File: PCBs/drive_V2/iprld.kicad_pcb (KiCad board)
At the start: 2 copper layers, 100 x 100 mm, 78 parts, among them IC1 W25Q16JVUXIQ_TR, IC2 ADS1115IDGSR, J1 SM06B-GHS-TB_LF__SN_, J10 XT60PW-F, J11 12401832E402A, J2 SM06B-GHS-TB_LF__SN_, J3 SM06B-GHS-TB_LF__SN_, J4 SM06B-GHS-TB_LF__SN_, J5 SM06B-GHS-TB_LF__SN_, J6 XT60PW-F, J7 SM06B-GHS-TB_LF__SN_, J8 XT60PW-F, J9 XT30PW-F, U1 AMS1117-3.3, U10 USBLC6-4SC6, U11 4N35, U12 4N35, U13 4N35, U14 4N35, U2 ESP32-S3, U3 4N35, U5 TCA9548APWR, U6 4N35, U7 4N35, U8 4N35, U9 AMS1117-5.0, Y1 7M40000010

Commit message: Add files via upload
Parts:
- moved U3 0.40 mm to (41.7, 19.6)
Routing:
- net /+FUSE_R: track 27.0 -> 30.6 mm
- net /+FUSE_L: track 17.9 -> 21.2 mm
- net /VBUS: track 20.4 -> 21.4 mm
- net /D+: track 82.7 -> 83.6 mm

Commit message: Add files via upload
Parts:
- moved D1 3.15 mm to (84.3, 83.8)
- moved U10 3.15 mm to (78.2, 83.6)
- moved J11 3.10 mm to (81.5, 93.8)
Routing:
- net /+FUSE_R: track 30.6 -> 26.6 mm
- net Net-(J11-CC2): track 16.0 -> 19.1 mm
- net GND: track 258.3 -> 261.4 mm
- net /D-: track 84.9 -> 87.2 mm
- net +5V: track 372.4 -> 373.7 mm
- net /D+: track 83.6 -> 84.9 mm
- net Net-(J11-CC1): track 16.8 -> 18.1 mm
- net +3.3V: vias 6 -> 8
- added copper zone on F.Cu, net +5V

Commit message: TEST1 - added a via
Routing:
- net GND: vias 45 -> 46
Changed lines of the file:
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@@
+	)
+	(via
+		(at 51.2 35.7)
+		(size 0.6)
+		(drill 0.3)
+		(layers "F.Cu" "B.Cu")
+		(free yes)
+		(net 1)
 	)
 	(via

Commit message: changed adc components
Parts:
- added C9: 1u, Capacitor_SMD:C_0603_1608Metric, F.Cu at (50.3, 54.8)
- added G***: LOGO, main_lib:IPRL_31mm, F.Cu at (78.0, 65.6)
- added R1: 10k, Resistor_SMD:R_0805_2012Metric, F.Cu at (50.2, 45.5)
- added R8: 10k, Resistor_SMD:R_0805_2012Metric, F.Cu at (50.3, 58.1)
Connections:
- IC2 pad 1: GND -> Net-(IC2-ADDR)
- IC2 pad 2: unconnected-(IC2-ALERT/RDY-Pad2) -> Net-(IC2-ALERT/RDY)
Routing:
- net Net-(IC2-ALERT/RDY): track 0.00 -> 12.2 mm, vias 0 -> 2
- net +3.3V: track 271.9 -> 278.9 mm
- net Net-(IC2-ADDR): track 0.00 -> 6.85 mm
- net GND: track 261.4 -> 256.4 mm

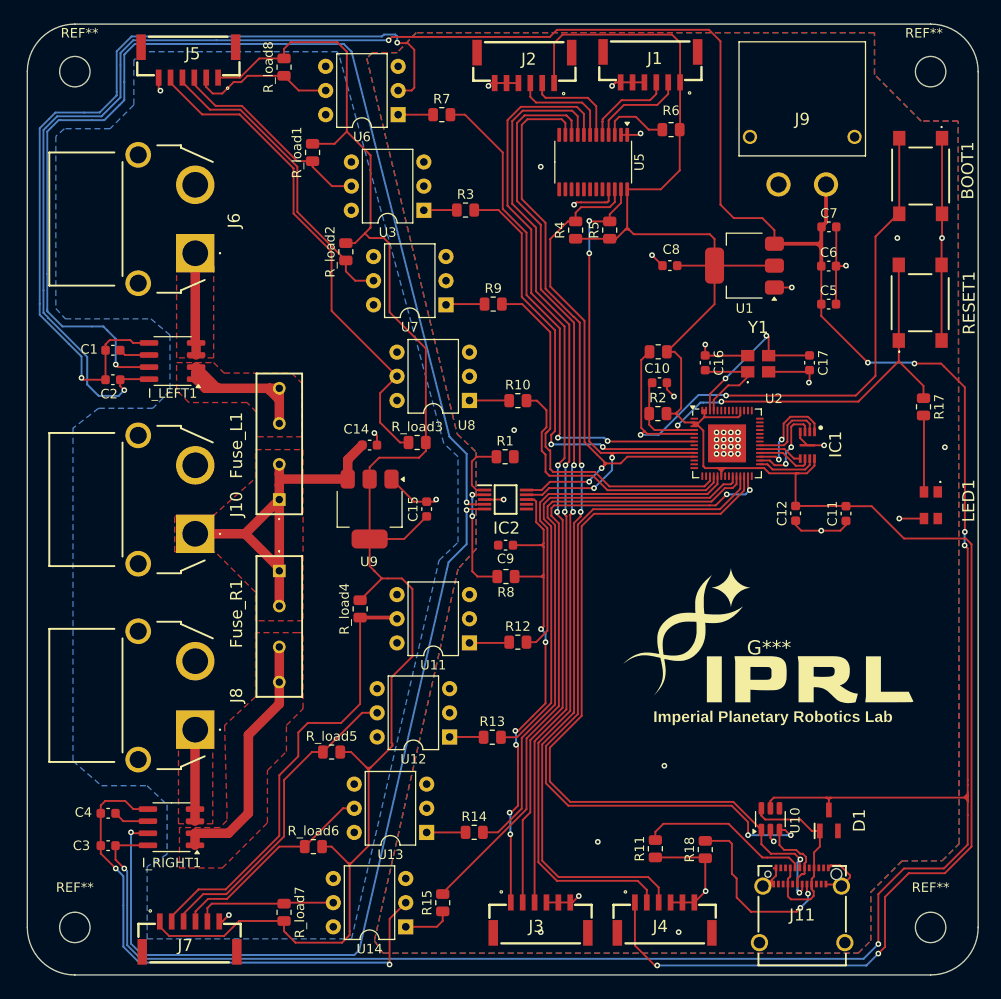
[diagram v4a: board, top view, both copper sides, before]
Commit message: New USB C footprint, changed XT inputs to male
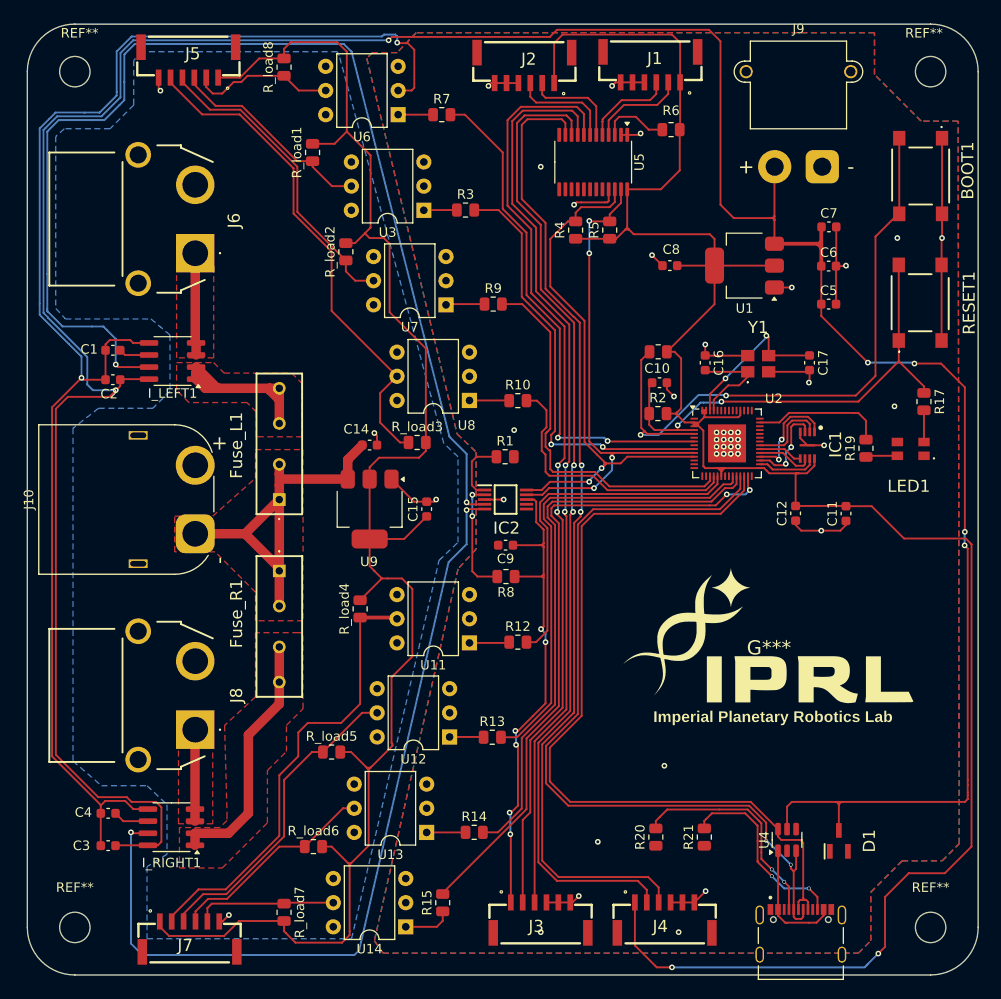
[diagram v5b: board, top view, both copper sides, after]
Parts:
- removed J11: 12401832E402A, iprl_footprints:12401832E402A
- removed R11, R18: 5.1k, Resistor_SMD:R_0805_2012Metric
- removed U10: USBLC6-4SC6, Package_TO_SOT_SMD:SOT-23-6
- added J12: TYPE-C-31-M-12, main_lib:TYPE-C-31-M-12, F.Cu at (81.3, 97.9)
- added R19: 56, Resistor_SMD:R_0805_2012Metric, F.Cu at (88.2, 44.6)
- added R20: 5.1k, Resistor_SMD:R_0805_2012Metric, F.Cu at (66.1, 85.5)
- added R21: 5.1k, Resistor_SMD:R_0805_2012Metric, F.Cu at (71.2, 85.5)
- added U4: USBLC6-4SC6, Package_TO_SOT_SMD:SOT-23-6, F.Cu at (79.9, 85.8)
- J10: footprint iprl_footprints:XT60PWF -> Connector_AMASS:AMASS_XT60PW-M_1x02_P7.20mm_Horizontal
- J9: footprint iprl_footprints:XT30PWF -> Connector_AMASS:AMASS_XT30PW-M_1x02_P2.50mm_Horizontal
- moved LED1 6.29 mm to (92.9, 44.7), turned to 0 degrees
- moved J9 4.96 mm to (83.6, 15.0)
- moved D1 2.39 mm to (85.3, 85.9)
- moved R17 0.55 mm to (94.3, 39.7)
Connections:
- LED1 pad 1: unconnected-(LED1-K_RED-Pad1) -> GND
- LED1 pad 2: unconnected-(LED1-A_RED-Pad2) -> Net-(LED1-A_RED)
- U2 pad 41: unconnected-(U2-GPIO36-Pad41) -> /LED_Red
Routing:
- net +5V: track 373.7 -> 325.1 mm, vias 8 -> 6
- net GND: track 256.4 -> 231.8 mm, vias 46 -> 42
- net Net-(J12-CC1): track 0.00 -> 23.3 mm, vias 0 -> 2
- net Net-(J12-CC2): track 0.00 -> 20.2 mm, vias 0 -> 2
- net Net-(J11-CC2): track 19.1 -> 0.00 mm, vias 2 -> 0
- net Net-(J11-CC1): track 18.1 -> 0.00 mm
- net /LED_Red: track 0.00 -> 13.9 mm
- net /VBUS: track 21.4 -> 12.9 mm
- net Net-(LED1-A_GREEN): track 8.06 -> 3.34 mm
- net Net-(LED1-A_RED): track 0.00 -> 3.35 mm
- net /D+: track 84.9 -> 87.3 mm, vias 2 -> 0
- net /D-: track 87.2 -> 88.8 mm
- net Net-(RESET1-NO_1): track 51.5 -> 51.0 mm
- removed copper zone on F.Cu, net +5V

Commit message: added connector names
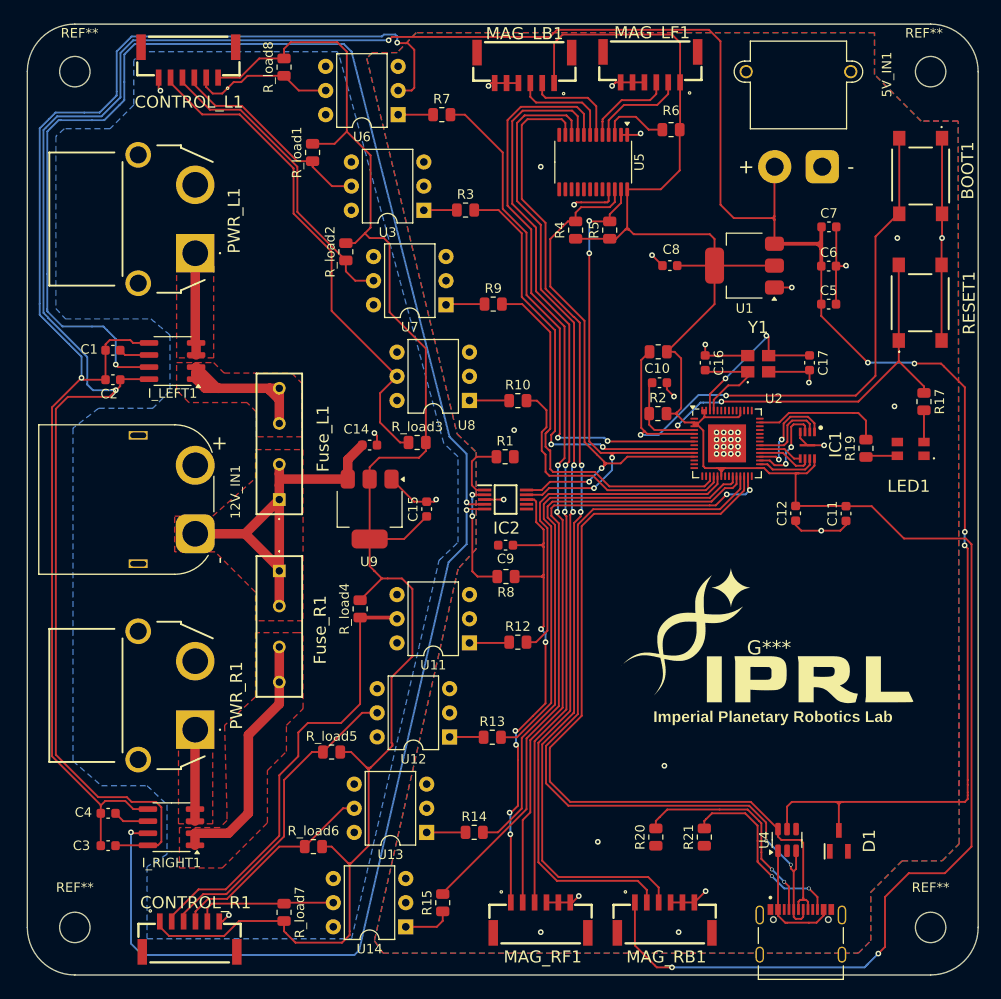
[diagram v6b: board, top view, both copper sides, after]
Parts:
- renumbered J10 to 12V_IN1, J9 to 5V_IN1, J5 to CONTROL_L1, J7 to CONTROL_R1, J2 to MAG_LB1, J1 to MAG_LF1, J4 to MAG_RB1, J3 to MAG_RF1, J6 to PWR_L1, J8 to PWR_R1
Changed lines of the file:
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@@
 		(descr "Connector XT30 Horizontal PCB Male, https://www.tme.eu/Document/6eb2005a51a52592b3f19e8a450c54c8/XT30PW-M.pdf")
 		(tags "RC Connector XT30")
-		(property "Reference" "J9"
-			(at -2.5 -14.5 0)
+		(property "Reference" "5V_IN1"
+			(at 6.8 -9.7 -90)
 			(layer "F.SilkS")
 			(effects
@@
 		(descr "XT60PW-F-4")
 		(tags "Connector")
-		(property "Reference" "J8"
+		(property "Reference" "PWR_R1"
 			(at 3.6 4.3375 -90)
 			(layer "F.SilkS")
@@
 		(descr "SM06B-GHS-TB")
 		(tags "Connector")
-		(property "Reference" "J2"
-			(at 4.91667 -1.78567 180)
+		(property "Reference" "MAG_LB1"
+			(at 5.35 0.9 0)
 			(layer "F.SilkS")
 			(effects
@@
 		(descr "SM06B-GHS-TB")
 		(tags "Connector")
-		(property "Reference" "J7"
-			(at 4.91667 -1.78567 0)
+		(property "Reference" "CONTROL_R1"
+			(at 6.0135 -6.273885 0)
 			(layer "F.SilkS")
 			(effects
@@
 		(descr "SM06B-GHS-TB")
 		(tags "Connector")
-		(property "Reference" "J1"
-			(at 4.91667 -1.78567 180)
+		(property "Reference" "MAG_LF1"
+			(at 5.2 0.926115 180)
 			(layer "F.SilkS")
 			(effects
@@
 		(tags "LED")
 		(property "Reference" "LED1"
-			(at -0.2 3.925 360)
+			(at -0.2 3.925 0)
 			(layer "F.SilkS")
 			(effects
@@
 		)
 		(property "Value" "AAA3528ESGCT"
-			(at 0.25 0 360)
+			(at 0.25 0 0)
 			(layer "F.SilkS")
 			(hide yes)
@@
 		)
 		(fp_text user "${REFERENCE}"
-			(at 0.25 0 360)
+			(at 0.25 0 0)
 			(layer "F.Fab")
 			(effects
@@
 		(tags "Undefined or Miscellaneous")
 		(property "Reference" "Fuse_L1"
-			(at 5.7 -4.5 -90)
+			(at 6.4 4.6 -90)
 			(layer "F.SilkS")
 			(effects
@@
 		(descr "SM06B-GHS-TB")
 		(tags "Connector")
-		(property "Reference" "J5"
-			(at 4.91667 -1.78567 180)
+		(property "Reference" "CONTROL_L1"
+			(at 5.3135 -6.873885 180)
 			(layer "F.SilkS")
 			(effects
@@
 		(descr "Connector XT60 Horizontal PCB Female, https://www.tme.eu/Document/b13629717d44ae038681dba08d18c0b6/XT60PW-M.pdf")
 		(tags "RC Connector XT60")
-		(property "Reference" "J10"
-			(at 3.6 -17.5 90)
+		(property "Reference" "12V_IN1"
+			(at 4.4 4.2375 90)
 			(layer "F.SilkS")
 			(effects
@@
 		(descr "SM06B-GHS-TB")
 		(tags "Connector")
-		(property "Reference" "J3"
-			(at 4.91667 -1.78567 0)
+		(property "Reference" "MAG_RF1"
+			(at 5.6 1.426115 0)
 			(layer "F.SilkS")
 			(effects
@@
 		)
 		(fp_text user "${REFERENCE}"
-			(at 4.91667 -1.78567 0)
+			(at 5.3135 -2.673885 0)
 			(layer "F.Fab")
 			(effects
@@
 		(descr "XT60PW-F-4")
 		(tags "Connector")
-		(property "Reference" "J6"
+		(property "Reference" "PWR_L1"
 			(at 3.4375 4.0875 -90)
 			(layer "F.SilkS")
@@
 		(tags "Undefined or Miscellaneous")
 		(property "Reference" "Fuse_R1"
-			(at 4.5 4.5 90)
+			(at 6.2 -4.3 90)
 			(layer "F.SilkS")
 			(effects
@@
 		(descr "SM06B-GHS-TB")
 		(tags "Connector")
-		(property "Reference" "J4"
-			(at 4.91667 -1.78567 0)
+		(property "Reference" "MAG_RB1"
+			(at 5.55 1.426115 0)
 			(layer "F.SilkS")
 			(effects
